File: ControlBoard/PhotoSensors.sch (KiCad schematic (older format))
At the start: 59 parts, among them J12 Conn_01x01, J13 Conn_01x01, J14 Conn_01x01, J15 Conn_01x01, J16 Conn_01x06, J17 Conn_01x06, J18 Conn_01x06, U10 LMT85, U11 74HC138, U12 4051, U13 4051, U2 LM358

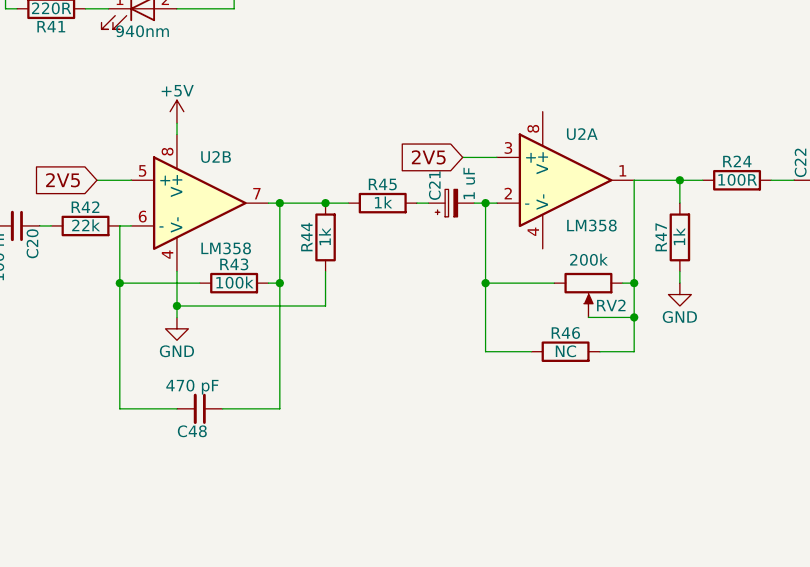
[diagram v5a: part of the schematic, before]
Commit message: Added some filter capacitors
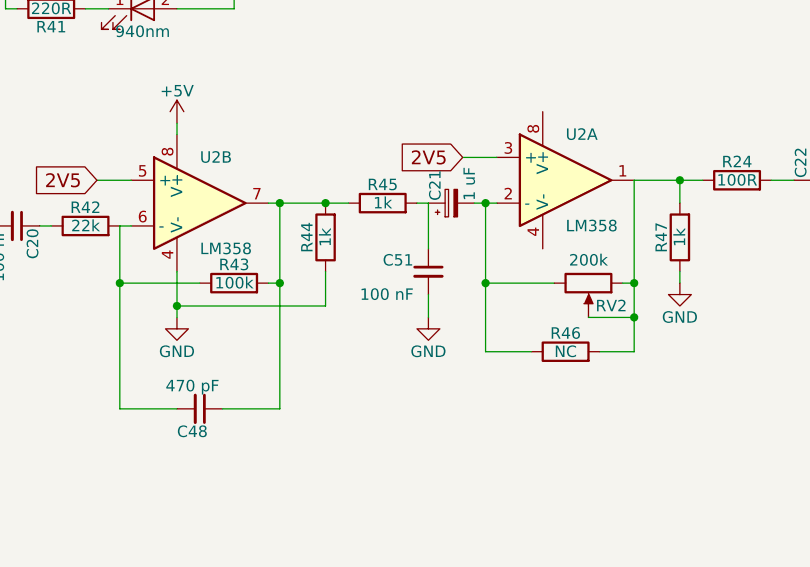
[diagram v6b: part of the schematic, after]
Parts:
- added C51: 100 nF, Capacitors_THT:C_Disc_D5.0mm_W2.5mm_P5.00mm, symbol C_Small
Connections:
- net GND: now also C51.2
- net at C21.1, R45.2: now also C51.1
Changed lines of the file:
@@
 $EndComp
 $Comp
-L +5V #PWR77
+L +5V #PWR78
 U 1 1 6147F8AB
 P 4850 2850
-F 0 "#PWR77" H 4850 2700 50  0001 C CNN
+F 0 "#PWR78" H 4850 2700 50  0001 C CNN
 F 1 "+5V" H 4850 2990 50  0000 C CNN
 F 2 "" H 4850 2850 50  0001 C CNN
@@
 $EndComp
 $Comp
-L GND #PWR78
+L GND #PWR79
 U 1 1 6147F8C9
 P 4850 4350
-F 0 "#PWR78" H 4850 4100 50  0001 C CNN
+F 0 "#PWR79" H 4850 4100 50  0001 C CNN
 F 1 "GND" H 4850 4200 50  0000 C CNN
 F 2 "" H 4850 4350 50  0001 C CNN
@@
 PHOTSELC
 $Comp
-L +5V #PWR73
+L +5V #PWR74
 U 1 1 6147FAC5
 P 4100 800
-F 0 "#PWR73" H 4100 650 50  0001 C CNN
+F 0 "#PWR74" H 4100 650 50  0001 C CNN
 F 1 "+5V" H 4100 940 50  0000 C CNN
 F 2 "" H 4100 800 50  0001 C CNN
@@
 $EndComp
 $Comp
-L GND #PWR74
+L GND #PWR75
 U 1 1 6147FAE8
 P 4100 2100
-F 0 "#PWR74" H 4100 1850 50  0001 C CNN
+F 0 "#PWR75" H 4100 1850 50  0001 C CNN
 F 1 "GND" H 4100 1950 50  0000 C CNN
 F 2 "" H 4100 2100 50  0001 C CNN
@@
 $EndComp
 $Comp
-L +5V #PWR84
+L +5V #PWR85
 U 1 1 6147FF6D
 P 6650 1100
-F 0 "#PWR84" H 6650 950 50  0001 C CNN
+F 0 "#PWR85" H 6650 950 50  0001 C CNN
 F 1 "+5V" H 6650 1240 50  0000 C CNN
 F 2 "" H 6650 1100 50  0001 C CNN
@@
 $EndComp
 $Comp
-L +5V #PWR58
+L +5V #PWR59
 U 1 1 614812EF
 P 1750 2400
-F 0 "#PWR58" H 1750 2250 50  0001 C CNN
+F 0 "#PWR59" H 1750 2250 50  0001 C CNN
 F 1 "+5V" H 1750 2540 50  0000 C CNN
 F 2 "" H 1750 2400 50  0001 C CNN
@@
 $EndComp
 $Comp
-L +5V #PWR62
+L +5V #PWR63
 U 1 1 61481486
 P 2050 700
-F 0 "#PWR62" H 2050 550 50  0001 C CNN
+F 0 "#PWR63" H 2050 550 50  0001 C CNN
 F 1 "+5V" H 2050 840 50  0000 C CNN
 F 2 "" H 2050 700 50  0001 C CNN
@@
 $EndComp
 $Comp
-L GND #PWR63
+L GND #PWR64
 U 1 1 614814CA
 P 2050 1150
-F 0 "#PWR63" H 2050 900 50  0001 C CNN
+F 0 "#PWR64" H 2050 900 50  0001 C CNN
 F 1 "GND" H 2050 1000 50  0000 C CNN
 F 2 "" H 2050 1150 50  0001 C CNN
@@
 $EndComp
 $Comp
-L GND #PWR72
+L GND #PWR73
 U 1 1 61481D45
 P 3800 4350
-F 0 "#PWR72" H 3800 4100 50  0001 C CNN
+F 0 "#PWR73" H 3800 4100 50  0001 C CNN
 F 1 "GND" H 3800 4200 50  0000 C CNN
 F 2 "" H 3800 4350 50  0001 C CNN
@@
 $EndComp
 $Comp
-L GND #PWR64
+L GND #PWR65
 U 1 1 61482BB1
 P 2200 4250
-F 0 "#PWR64" H 2200 4000 50  0001 C CNN
+F 0 "#PWR65" H 2200 4000 50  0001 C CNN
 F 1 "GND" H 2200 4100 50  0000 C CNN
 F 2 "" H 2200 4250 50  0001 C CNN
@@
 $EndComp
 $Comp
-L GND #PWR59
+L GND #PWR60
 U 1 1 61482FE8
 P 1850 4250
-F 0 "#PWR59" H 1850 4000 50  0001 C CNN
+F 0 "#PWR60" H 1850 4000 50  0001 C CNN
 F 1 "GND" H 1850 4100 50  0000 C CNN
 F 2 "" H 1850 4250 50  0001 C CNN
@@
 $EndComp
 $Comp
-L GND #PWR55
+L GND #PWR56
 U 1 1 614831F0
 P 1500 4250
-F 0 "#PWR55" H 1500 4000 50  0001 C CNN
+F 0 "#PWR56" H 1500 4000 50  0001 C CNN
 F 1 "GND" H 1500 4100 50  0000 C CNN
 F 2 "" H 1500 4250 50  0001 C CNN
@@
 $EndComp
 $Comp
-L GND #PWR54
+L GND #PWR55
 U 1 1 614834E7
 P 1150 4250
-F 0 "#PWR54" H 1150 4000 50  0001 C CNN
+F 0 "#PWR55" H 1150 4000 50  0001 C CNN
 F 1 "GND" H 1150 4100 50  0000 C CNN
 F 2 "" H 1150 4250 50  0001 C CNN
@@
 $EndComp
 $Comp
-L GND #PWR83
+L GND #PWR84
 U 1 1 614843BC
 P 6400 3350
-F 0 "#PWR83" H 6400 3100 50  0001 C CNN
+F 0 "#PWR84" H 6400 3100 50  0001 C CNN
 F 1 "GND" H 6400 3200 50  0000 C CNN
 F 2 "" H 6400 3350 50  0001 C CNN
@@
 $EndComp
 $Comp
-L +5V #PWR82
+L +5V #PWR83
 U 1 1 614844BC
 P 6400 2500
-F 0 "#PWR82" H 6400 2350 50  0001 C CNN
+F 0 "#PWR83" H 6400 2350 50  0001 C CNN
 F 1 "+5V" H 6400 2640 50  0000 C CNN
 F 2 "" H 6400 2500 50  0001 C CNN
@@
 $EndComp
 $Comp
-L GND #PWR85
+L GND #PWR87
 U 1 1 614885D2
 P 8600 3200
-F 0 "#PWR85" H 8600 2950 50  0001 C CNN
+F 0 "#PWR87" H 8600 2950 50  0001 C CNN
 F 1 "GND" H 8600 3050 50  0000 C CNN
 F 2 "" H 8600 3200 50  0001 C CNN
@@
 $EndComp
 $Comp
-L GND #PWR86
+L GND #PWR88
 U 1 1 61489586
 P 9450 3200
-F 0 "#PWR86" H 9450 2950 50  0001 C CNN
+F 0 "#PWR88" H 9450 2950 50  0001 C CNN
 F 1 "GND" H 9450 3050 50  0000 C CNN
 F 2 "" H 9450 3200 50  0001 C CNN
@@
 $EndComp
 $Comp
-L GND #PWR87
+L GND #PWR89
 U 1 1 61489C2F
 P 9950 3200
-F 0 "#PWR87" H 9950 2950 50  0001 C CNN
+F 0 "#PWR89" H 9950 2950 50  0001 C CNN
 F 1 "GND" H 9950 3050 50  0000 C CNN
 F 2 "" H 9950 3200 50  0001 C CNN
@@
 $EndComp
 $Comp
-L GND #PWR88
+L GND #PWR90
 U 1 1 6148A4C2
 P 10250 3200
-F 0 "#PWR88" H 10250 2950 50  0001 C CNN
+F 0 "#PWR90" H 10250 2950 50  0001 C CNN
 F 1 "GND" H 10250 3050 50  0000 C CNN
 F 2 "" H 10250 3200 50  0001 C CNN
@@
 $EndComp
 $Comp
-L +5V #PWR79
+L +5V #PWR80
 U 1 1 614BCEBF
 P 5150 5850
-F 0 "#PWR79" H 5150 5700 50  0001 C CNN
+F 0 "#PWR80" H 5150 5700 50  0001 C CNN
 F 1 "+5V" H 5150 5990 50  0000 C CNN
 F 2 "" H 5150 5850 50  0001 C CNN
@@
 $EndComp
 $Comp
-L GND #PWR80
+L GND #PWR81
 U 1 1 614BCEC5
 P 5150 7350
-F 0 "#PWR80" H 5150 7100 50  0001 C CNN
+F 0 "#PWR81" H 5150 7100 50  0001 C CNN
 F 1 "GND" H 5150 7200 50  0000 C CNN
 F 2 "" H 5150 7350 50  0001 C CNN
@@
 $EndComp
 $Comp
-L GND #PWR75
+L GND #PWR76
 U 1 1 614BCF0A
 P 4100 7350
-F 0 "#PWR75" H 4100 7100 50  0001 C CNN
+F 0 "#PWR76" H 4100 7100 50  0001 C CNN
 F 1 "GND" H 4100 7200 50  0000 C CNN
 F 2 "" H 4100 7350 50  0001 C CNN
@@
 LIGHTLEVEL
 $Comp
-L +5V #PWR60
+L +5V #PWR61
 U 1 1 614C0527
 P 1950 4950
-F 0 "#PWR60" H 1950 4800 50  0001 C CNN
+F 0 "#PWR61" H 1950 4800 50  0001 C CNN
 F 1 "+5V" H 1950 5090 50  0000 C CNN
 F 2 "" H 1950 4950 50  0001 C CNN
@@
 $EndComp
 $Comp
-L GND #PWR68
+L GND #PWR69
 U 1 1 614C2B73
 P 3000 7100
-F 0 "#PWR68" H 3000 6850 50  0001 C CNN
+F 0 "#PWR69" H 3000 6850 50  0001 C CNN
 F 1 "GND" H 3000 6950 50  0000 C CNN
 F 2 "" H 3000 7100 50  0001 C CNN
@@
 $EndComp
 $Comp
-L GND #PWR66
+L GND #PWR67
 U 1 1 614C2DE0
 P 2650 7100
-F 0 "#PWR66" H 2650 6850 50  0001 C CNN
+F 0 "#PWR67" H 2650 6850 50  0001 C CNN
 F 1 "GND" H 2650 6950 50  0000 C CNN
 F 2 "" H 2650 7100 50  0001 C CNN
@@
 $EndComp
 $Comp
-L GND #PWR65
+L GND #PWR66
 U 1 1 614C2FCF
 P 2300 7100
-F 0 "#PWR65" H 2300 6850 50  0001 C CNN
+F 0 "#PWR66" H 2300 6850 50  0001 C CNN
 F 1 "GND" H 2300 6950 50  0000 C CNN
 F 2 "" H 2300 7100 50  0001 C CNN
@@
 $EndComp
 $Comp
-L GND #PWR61
+L GND #PWR62
 U 1 1 614C31BF
 P 1950 7100
-F 0 "#PWR61" H 1950 6850 50  0001 C CNN
+F 0 "#PWR62" H 1950 6850 50  0001 C CNN
 F 1 "GND" H 1950 6950 50  0000 C CNN
 F 2 "" H 1950 7100 50  0001 C CNN
@@
 $EndComp
 $Comp
-L GND #PWR57
+L GND #PWR58
 U 1 1 614CA69F
 P 1500 6700
-F 0 "#PWR57" H 1500 6450 50  0001 C CNN
+F 0 "#PWR58" H 1500 6450 50  0001 C CNN
 F 1 "GND" H 1500 6550 50  0000 C CNN
 F 2 "" H 1500 6700 50  0001 C CNN
@@
 $EndComp
 $Comp
-L +5V #PWR56
+L +5V #PWR57
 U 1 1 614CA9A1
 P 1500 5900
-F 0 "#PWR56" H 1500 5750 50  0001 C CNN
+F 0 "#PWR57" H 1500 5750 50  0001 C CNN
 F 1 "+5V" H 1500 6040 50  0000 C CNN
 F 2 "" H 1500 5900 50  0001 C CNN
@@
 $EndComp
 $Comp
-L +5V #PWR76
+L +5V #PWR77
 U 1 1 6148B87D
 P 4800 850
-F 0 "#PWR76" H 4800 700 50  0001 C CNN
+F 0 "#PWR77" H 4800 700 50  0001 C CNN
 F 1 "+5V" H 4800 990 50  0000 C CNN
 F 2 "" H 4800 850 50  0001 C CNN
@@
 $EndComp
 $Comp
-L GND #PWR70
+L GND #PWR71
 U 1 1 6148D946
 P 3450 4450
-F 0 "#PWR70" H 3450 4200 50  0001 C CNN
+F 0 "#PWR71" H 3450 4200 50  0001 C CNN
 F 1 "GND" H 3450 4300 50  0000 C CNN
 F 2 "" H 3450 4450 50  0001 C CNN
@@
 $EndComp
 $Comp
-L +5V #PWR67
+L +5V #PWR68
 U 1 1 6148DEB8
 P 2950 3850
-F 0 "#PWR67" H 2950 3700 50  0001 C CNN
+F 0 "#PWR68" H 2950 3700 50  0001 C CNN
 F 1 "+5V" H 2950 3990 50  0000 C CNN
 F 2 "" H 2950 3850 50  0001 C CNN
@@
 $EndComp
 $Comp
-L GND #PWR81
+L GND #PWR82
 U 1 1 61482B42
 P 5500 700
-F 0 "#PWR81" H 5500 450 50  0001 C CNN
+F 0 "#PWR82" H 5500 450 50  0001 C CNN
 F 1 "GND" H 5500 550 50  0000 C CNN
 F 2 "" H 5500 700 50  0001 C CNN
@@
 	3850 6250 3850 5400
 $Comp
-L GND #PWR71
+L GND #PWR72
 U 1 1 61484CD9
 P 3650 5800
-F 0 "#PWR71" H 3650 5550 50  0001 C CNN
+F 0 "#PWR72" H 3650 5550 50  0001 C CNN
 F 1 "GND" H 3650 5650 50  0000 C CNN
 F 2 "" H 3650 5800 50  0001 C CNN
@@
 	3650 5800 3650 5400
 $Comp
-L +5V #PWR69
+L +5V #PWR70
 U 1 1 61484F3C
 P 3400 5100
-F 0 "#PWR69" H 3400 4950 50  0001 C CNN
+F 0 "#PWR70" H 3400 4950 50  0001 C CNN
 F 1 "+5V" H 3400 5240 50  0000 C CNN
 F 2 "" H 3400 5100 50  0001 C CNN
@@
 	6150 3750 6400 3750
 Connection ~ 6150 3200
+$Comp
+L GND #PWR86
+U 1 1 61DD3A58
+P 7500 3350
+F 0 "#PWR86" H 7500 3100 50  0001 C CNN
+F 1 "GND" H 7500 3200 50  0000 C CNN
+F 2 "" H 7500 3350 50  0001 C CNN
+F 3 "" H 7500 3350 50  0001 C CNN
+	1    7500 3350
+	1    0    0    -1
+$EndComp
+Wire Wire Line
+	7500 3350 7500 3250
+Wire Wire Line
+	7500 3050 7500 2850
+$Comp
+L C_Small C51
+U 1 1 61DD3DCA
+P 7500 3150
+F 0 "C51" H 7300 3200 50  0000 L CNN
+F 1 "100 nF" H 7200 3050 50  0000 L CNN
+F 2 "Capacitors_THT:C_Disc_D5.0mm_W2.5mm_P5.00mm" H 7500 3150 50  0001 C CNN
+F 3 "" H 7500 3150 50  0001 C CNN
+	1    7500 3150
+	1    0    0    -1
+$EndComp
 $EndSCHEMATC
